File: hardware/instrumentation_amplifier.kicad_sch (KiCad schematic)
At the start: 42 parts, among them U10 MCP6001-OT, U3 MCP6N11-010, U4 MCP4542, U9 MCP6001-OT

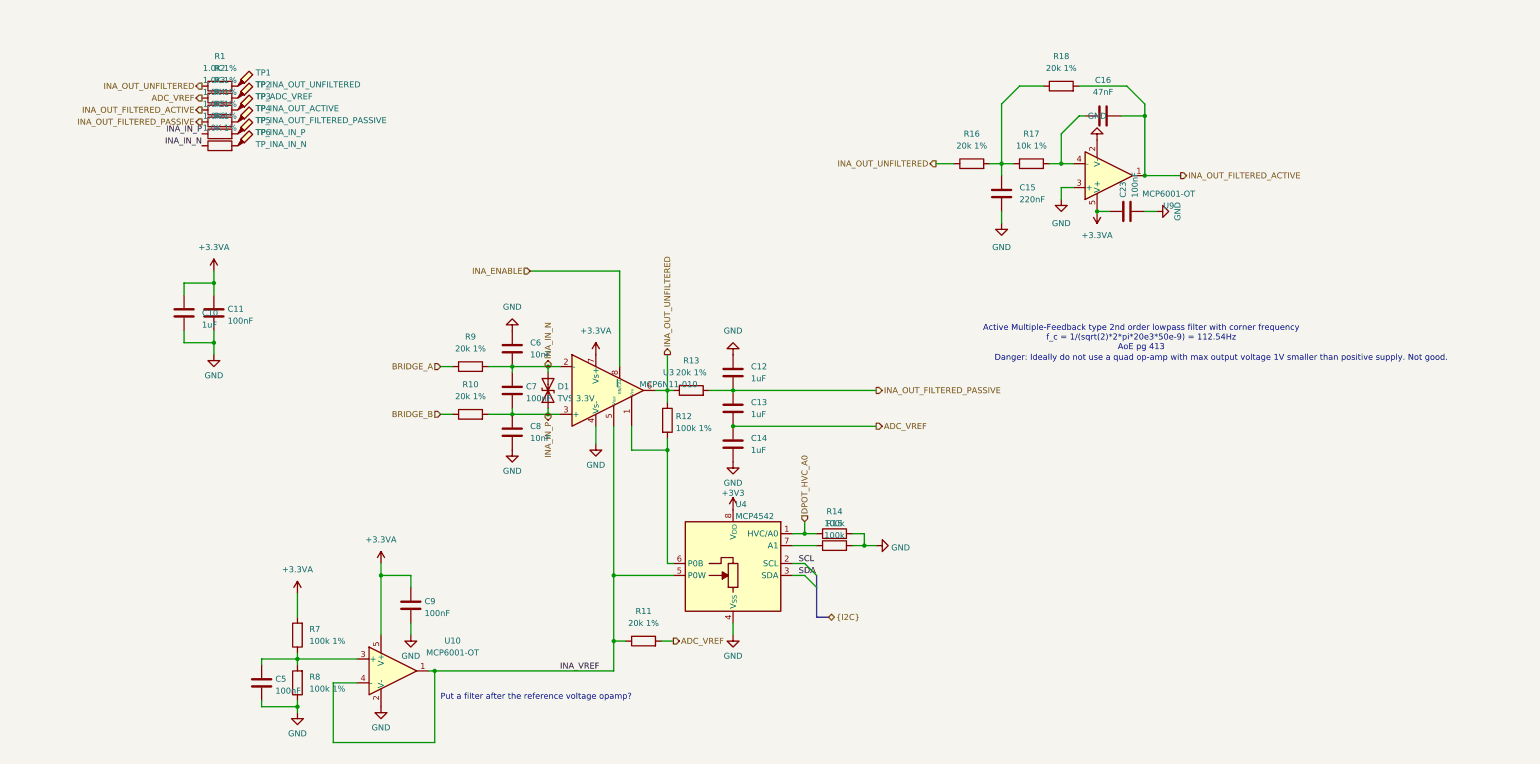
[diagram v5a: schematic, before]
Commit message: Added solder bridges and calculated resistor values for INA
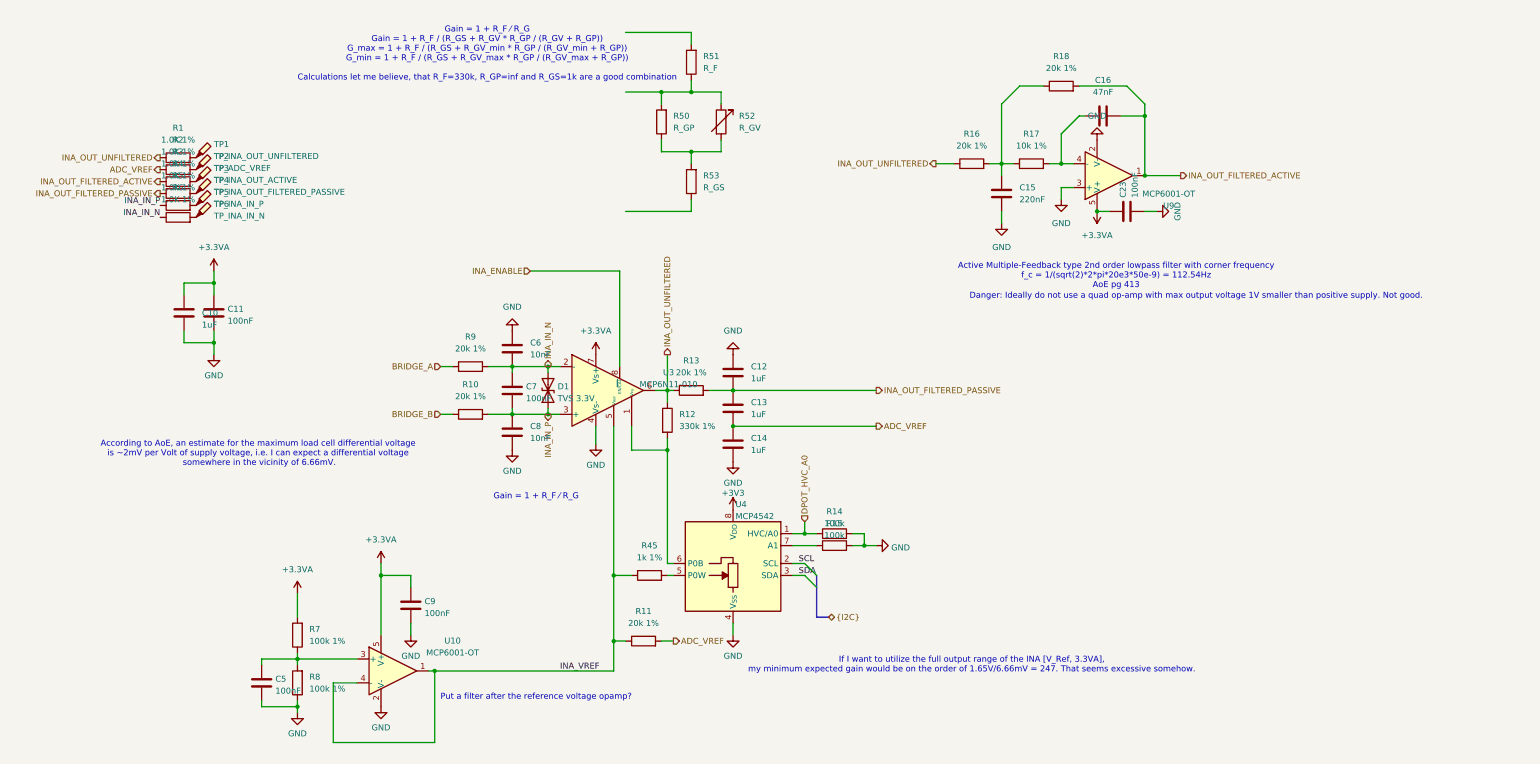
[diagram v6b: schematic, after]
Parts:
- added R45: 1k 1%, Resistor_SMD:R_0603_1608Metric, symbol Device:R
- added R50: R_GP, Resistor_SMD:R_0603_1608Metric, symbol Device:R
- added R51: R_F, Resistor_SMD:R_0603_1608Metric, symbol Device:R
- added R52: R_GV, symbol Device:R_Variable
- added R53: R_GS, Resistor_SMD:R_0603_1608Metric, symbol Device:R
- R12: value 100k 1% -> 330k 1%
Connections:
- net INA_VREF: now also R45.1; no longer U4.5 (P0W)
- new net: R45.2, U4.5 (P0W)
- new net: R50.1, R52.2, R53.2
- new net: R50.2, R51.1, R52.1
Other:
- note added: "According to AoE, an estimate for the maximum load cell differential voltage is ~2mV per Volt of supply voltage, i.e. I can expect a differential voltage somewhere in the vicinity of 6.66mV."
- note added: "Gain = 1 + R_F ⁄ R_G"
- note added: "Gain = 1 + R_F ⁄ R_G Gain = 1 + R_F / (R_GS + R_GV * R_GP / (R_GV + R_GP)) G_max = 1 + R_F / (R_GS + R_GV_min * R_GP / (R_GV_min + R_GP)) G_min = 1 + R_F / (R_GS + R_GV_max * R_GP / (R_GV_max + R_GP)) Calculations let me believe, that R_F=330k, R_GP=inf and R_GS=1k are a good combination"
- note added: "If I want to utilize the full output range of the INA [V_Ref, 3.3VA], my minimum expected gain would be on the order of 1.65V/6.66mV = 247. That seems excessive somehow."
- moved on the sheet: R1, R2, R3, R4, R5, R6, TP1, TP2, TP3, TP4, TP5, TP6

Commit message: Realized that 5V to VBat pin would fry the uC and abandoned ultra-low power design. Deferred to next revision.
A
A
A
A
A
A
A
A
A
A
A
A
A
A
A
A
A
A
B
B
B
B
B
B
B
B
B
B
B
B
B
B
B
A
A
A
A
A
A
A
A
A
A
A
A
A
A
P
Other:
- note added: "According to AoE, an estimate for the maximum load cell differential voltage is ~2mV per Volt of supply voltage, i.e. I can expect a differential voltage in the range +-6.66mV."
- note removed: "According to AoE, an estimate for the maximum load cell differential voltage is ~2mV per Volt of supply voltage, i.e. I can expect a differential voltage somewhere in the vicinity of 6.66mV."
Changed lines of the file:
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@@
 		)
 	)
-	(text "According to AoE, an estimate for the maximum load cell differential voltage\nis ~2mV per Volt of supply voltage, i.e. I can expect a differential voltage\n somewhere in the vicinity of 6.66mV."
+	(text "According to AoE, an estimate for the maximum load cell differential voltage\nis ~2mV per Volt of supply voltage, i.e. I can expect a differential voltage\n in the range +-6.66mV."
 		(exclude_from_sim no)
 		(at 66.548 108.712 0)

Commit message: Ran electrical check on schematic and implemented corrections
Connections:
- net ADC_VREF: now also R53.1
- net INA_OUT_UNFILTERED: now also R51.2
- net INA_FB: now reaches R50.2, R51.1, R52.1
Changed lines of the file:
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@@
 	(text "Gain = 1 + R_F ⁄ R_G\nGain = 1 + R_F / (R_GS + R_GV * R_GP / (R_GV + R_GP))\nG_max = 1 + R_F / (R_GS + R_GV_min * R_GP / (R_GV_min + R_GP))\nG_min = 1 + R_F / (R_GS + R_GV_max * R_GP / (R_GV_max + R_GP))\n\nCalculations let me believe, that R_F=330k, R_GP=inf and R_GS=1k are a good combination"
 		(exclude_from_sim no)
-		(at 115.316 23.622 0)
+		(at 94.996 20.828 0)
 		(effects
 			(font
@@
 	)
 	(junction
+		(at 165.1 31.75)
+		(diameter 0)
+		(color 0 0 0 0)
+	)
+	(junction
 		(at 128.27 90.17)
 		(diameter 0)
@@
 	(junction
 		(at 57.15 72.39)
-		(diameter 0)
-		(color 0 0 0 0)
-	)
-	(junction
-		(at 152.4 31.75)
 		(diameter 0)
 		(color 0 0 0 0)
@@
 	(wire
 		(pts
+			(xy 158.75 57.15) (xy 168.91 57.15)
+		)
+		(stroke
+			(width 0)
+			(type default)
+		)
+	)
+	(wire
+		(pts
 			(xy 138.43 102.87) (xy 138.43 106.68)
 		)
@@
 	(wire
 		(pts
-			(xy 144.78 31.75) (xy 152.4 31.75)
-		)
-		(stroke
-			(width 0)
-			(type default)
-		)
-	)
-	(wire
-		(pts
-			(xy 144.78 19.05) (xy 158.75 19.05)
-		)
-		(stroke
-			(width 0)
-			(type default)
-		)
-	)
-	(wire
-		(pts
 			(xy 142.24 102.87) (xy 142.24 134.62)
 		)
@@
 	(wire
 		(pts
-			(xy 144.78 57.15) (xy 158.75 57.15)
+			(xy 165.1 31.75) (xy 167.64 31.75)
 		)
 		(stroke
@@
 		(pts
 			(xy 165.1 44.45) (xy 165.1 41.91)
+		)
+		(stroke
+			(width 0)
+			(type default)
+		)
+	)
+	(wire
+		(pts
+			(xy 158.75 19.05) (xy 167.64 19.05)
 		)
 		(stroke
@@
 	(label "INA_VREF"
 		(at 130.81 154.94 0)
+		(effects
+			(font
+				(size 1.27 1.27)
+			)
+			(justify left bottom)
+		)
+	)
+	(label "INA_FB"
+		(at 167.64 31.75 0)
 		(effects
 			(font
@@
 		(effects
 			(font
+				(size 1.27 1.27)
+			)
+			(justify left)
+		)
+	)
+	(hierarchical_label "INA_OUT_UNFILTERED"
+		(shape output)
+		(at 167.64 19.05 0)
+		(effects
+			(font
+				(size 1.27 1.27)
+			)
+			(justify left)
+		)
+	)
+	(hierarchical_label "ADC_VREF"
+		(shape output)
+		(at 168.91 57.15 0)
+		(effects
+			(font
